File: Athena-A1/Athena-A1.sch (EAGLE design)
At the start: 86 parts, among them J1 MF-CON-MICROUSB-RIGHT, J2 TC2030-IDC-NL, J3 MF-CON-2.54mm-01x08, J4 MF-CON-2.54mm-01x08, J5 MF-CON-2.54mm-01x07, SW1 MF-SW-TACT-6MM, SW2 MF-SW-TACT-6MM, U1 PRTR5V0U2X,215, U2 MCP73831T-2ACI/OT, U3 AP2112K-3.3TRG1, U4 RT9080-18GJ5, U5 MK22FN128VLH10, U6 FE310, U7 32MBit, X1 JST 2-Pin, X2 MIKROE_CLICKMINI, Y1 TSX-3225-16.0000MF18X-AC0, Y2 KX3211A0032.768000

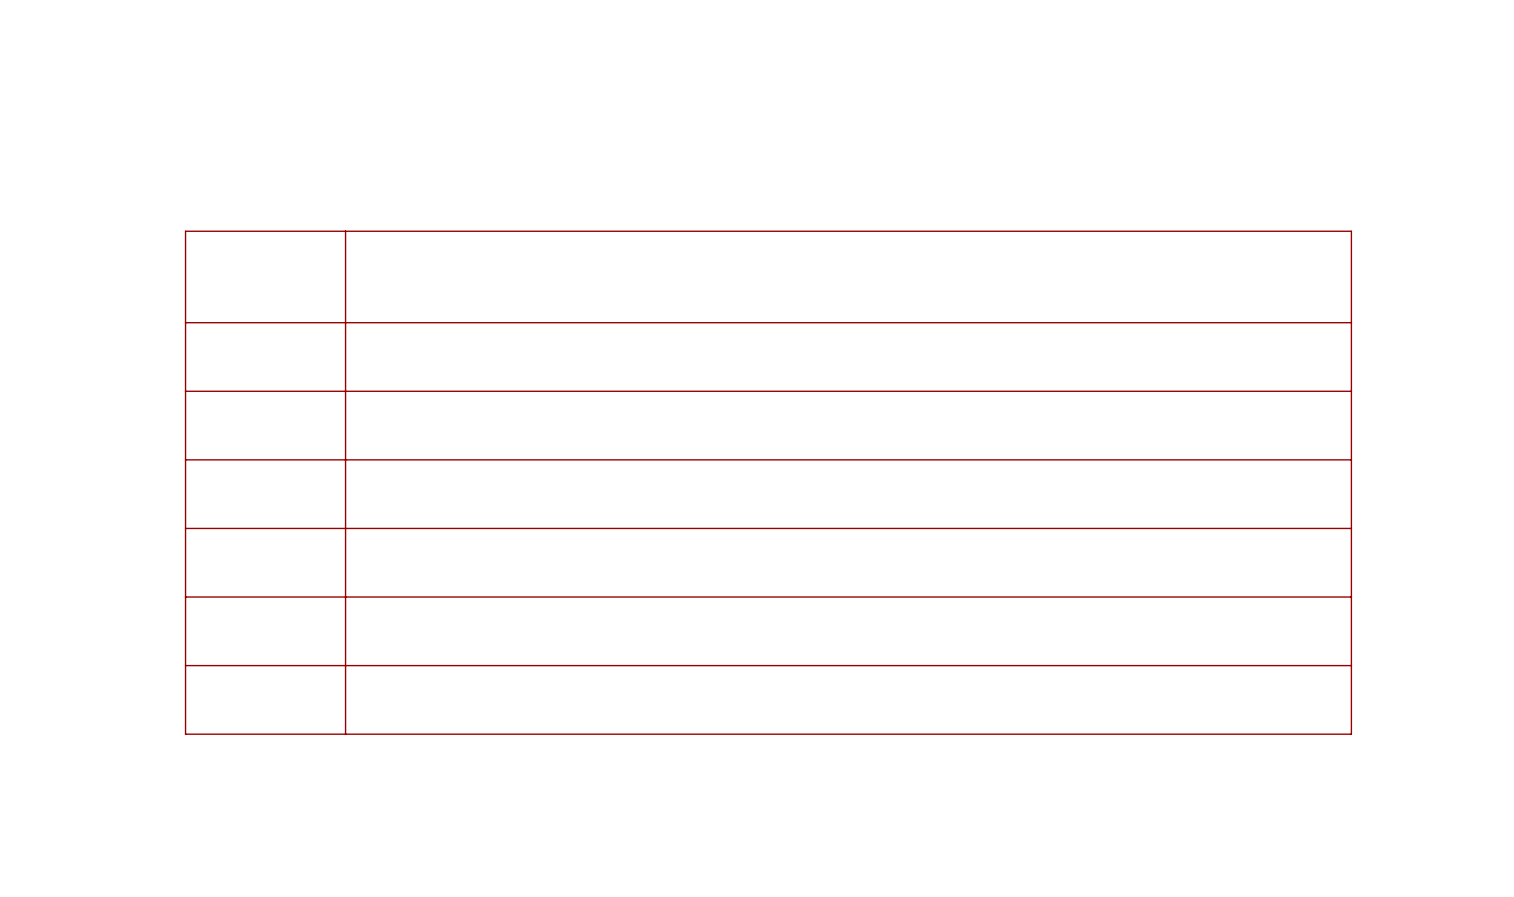
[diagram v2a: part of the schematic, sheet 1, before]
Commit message: Moved pours outside dimension
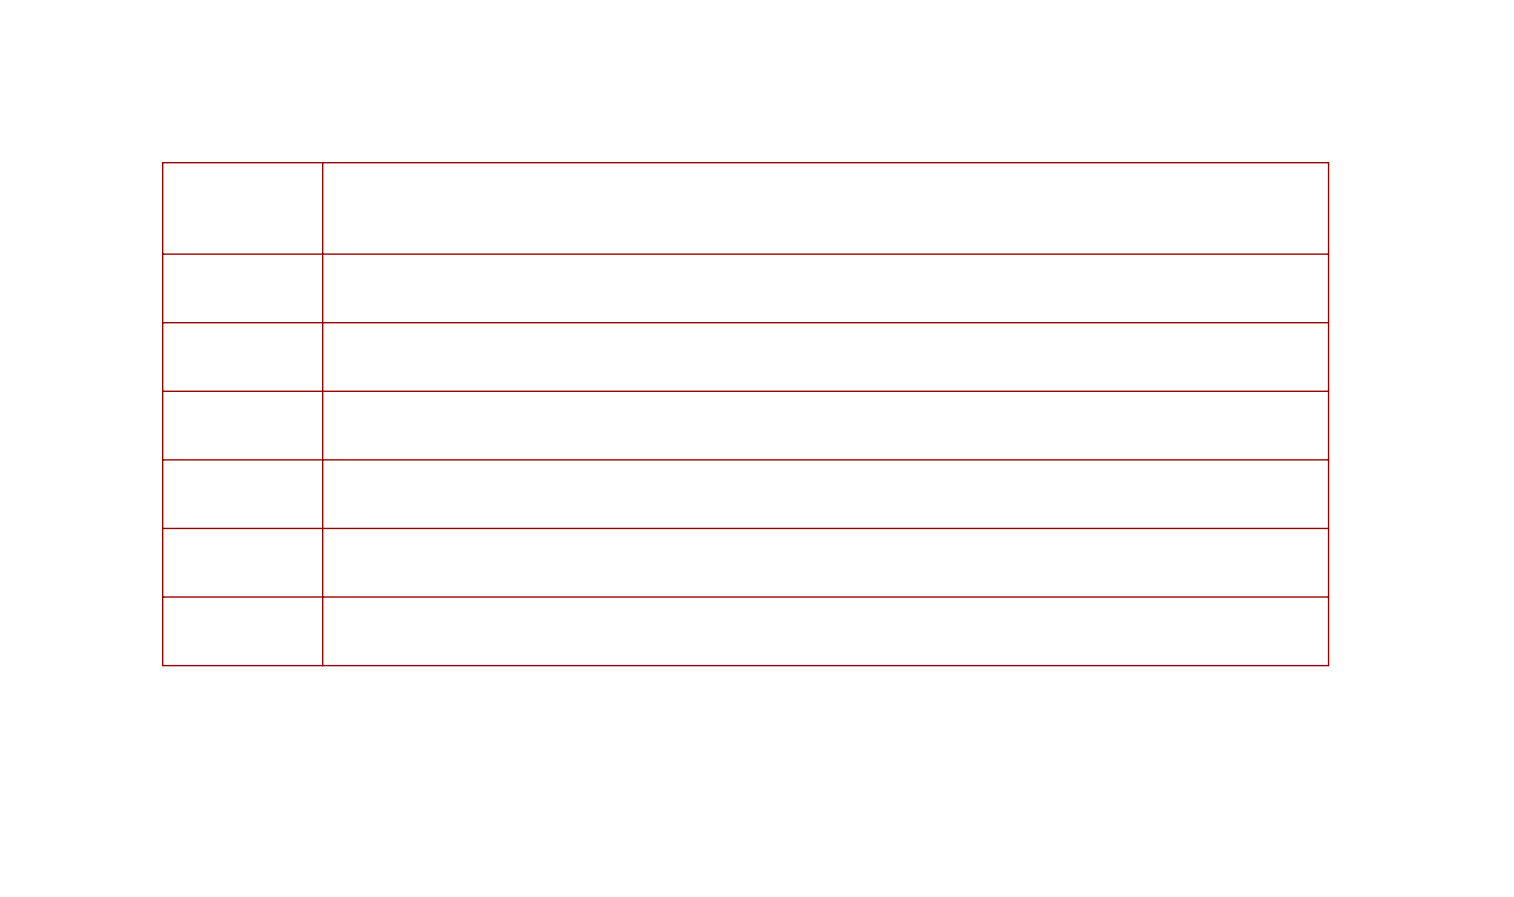
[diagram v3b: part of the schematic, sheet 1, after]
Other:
- note added: "Copyright © 2022 Rice University Permission is hereby granted, free of charge, to any person obtaining a copy of this design and associated documentation files (the “Design”), to deal in the Design without restriction, including without limitation the rights to use, copy, modify, merge, publish, distribute, sublicense, and/or sell copies of the Design, and to permit persons to whom the Design is 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"
- note removed: "ADD A COPYRIGHT AND LICENSE STATEMENT HERE"
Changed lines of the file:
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@@
 <text x="71.12" y="154.94" size="5.08" layer="150">Athena Design Rev. A1 Schematic</text>
 <text x="210.82" y="2.54" size="2.1844" layer="150">Designed in EAGLE 9.6.2.</text>
-<text x="63.5" y="109.22" size="2.54" layer="150" font="vector">The first RISC-V development board at Rice University, featuring the SiFive FE310
+<text x="60.96" y="114.3" size="2.54" layer="150" font="vector">The first RISC-V development board at Rice University, featuring the SiFive FE310
 microprocessor, Athena is a prototyping and experimental platform for education
 and research at Rice.  It is intended to be used in undergraduate lab courses and
 in VIP projects, therefore the design focus is on debug capability and I/O access.</text>
-<text x="114.3" y="91.44" size="2.54" layer="150" ratio="12">July 25, 2022</text>
+<text x="111.76" y="99.06" size="2.54" layer="150" ratio="12">July 25, 2022</text>
 <wire x1="0" y1="0" x2="0" y2="185.42" width="0.508" layer="94"/>
 <wire x1="248.92" y1="185.42" x2="248.92" y2="0" width="0.508" layer="94"/>
 <wire x1="0" y1="185.42" x2="248.92" y2="185.42" width="0.508" layer="94"/>
 <wire x1="0" y1="0" x2="248.92" y2="0" width="0.508" layer="94"/>
-<wire x1="63.5" y1="81.28" x2="81.28" y2="81.28" width="0.1524" layer="94"/>
-<wire x1="81.28" y1="81.28" x2="193.04" y2="81.28" width="0.1524" layer="94"/>
-<wire x1="193.04" y1="81.28" x2="193.04" y2="71.12" width="0.1524" layer="94"/>
-<wire x1="193.04" y1="71.12" x2="193.04" y2="63.5" width="0.1524" layer="94"/>
-<wire x1="193.04" y1="63.5" x2="193.04" y2="55.88" width="0.1524" layer="94"/>
-<wire x1="193.04" y1="55.88" x2="193.04" y2="48.26" width="0.1524" layer="94"/>
-<wire x1="193.04" y1="48.26" x2="193.04" y2="40.64" width="0.1524" layer="94"/>
-<wire x1="193.04" y1="40.64" x2="193.04" y2="33.02" width="0.1524" layer="94"/>
-<wire x1="193.04" y1="33.02" x2="193.04" y2="25.4" width="0.1524" layer="94"/>
-<wire x1="193.04" y1="25.4" x2="81.28" y2="25.4" width="0.1524" layer="94"/>
-<wire x1="81.28" y1="25.4" x2="63.5" y2="25.4" width="0.1524" layer="94"/>
-<wire x1="63.5" y1="25.4" x2="63.5" y2="33.02" width="0.1524" layer="94"/>
-<wire x1="63.5" y1="33.02" x2="63.5" y2="40.64" width="0.1524" layer="94"/>
-<wire x1="63.5" y1="40.64" x2="63.5" y2="48.26" width="0.1524" layer="94"/>
-<wire x1="63.5" y1="48.26" x2="63.5" y2="55.88" width="0.1524" layer="94"/>
-<wire x1="63.5" y1="55.88" x2="63.5" y2="63.5" width="0.1524" layer="94"/>
-<wire x1="63.5" y1="63.5" x2="63.5" y2="71.12" width="0.1524" layer="94"/>
-<wire x1="63.5" y1="71.12" x2="63.5" y2="81.28" width="0.1524" layer="94"/>
-<wire x1="63.5" y1="71.12" x2="193.04" y2="71.12" width="0.1524" layer="94"/>
-<wire x1="81.28" y1="81.28" x2="81.28" y2="25.4" width="0.1524" layer="94"/>
-<wire x1="63.5" y1="63.5" x2="193.04" y2="63.5" width="0.1524" layer="94"/>
-<wire x1="63.5" y1="55.88" x2="193.04" y2="55.88" width="0.1524" layer="94"/>
-<wire x1="63.5" y1="48.26" x2="193.04" y2="48.26" width="0.1524" layer="94"/>
-<wire x1="63.5" y1="40.64" x2="193.04" y2="40.64" width="0.1524" layer="94"/>
-<wire x1="63.5" y1="33.02" x2="193.04" y2="33.02" width="0.1524" layer="94"/>
-<text x="66.04" y="73.66" size="2.54" layer="150" font="vector" ratio="12">Sheet</text>
-<text x="66.04" y="66.04" size="2.54" layer="150" ratio="12">1</text>
-<text x="86.36" y="58.42" size="2.54" layer="150" ratio="12">Power: USB, Charging, Voltage Regulators</text>
-<text x="86.36" y="50.8" size="2.54" layer="150" ratio="12">Debug Control: MK22 Processor</text>
-<text x="86.36" y="66.04" size="2.54" layer="150" ratio="12">Cover Page</text>
-<text x="86.36" y="43.18" size="2.54" layer="150" ratio="12">Main Processor: SiFive FE310, the RISC-V MCU</text>
-<text x="86.36" y="35.56" size="2.54" layer="150" ratio="12">Peripherals: Oscillators, Flash Memory</text>
-<text x="86.36" y="27.94" size="2.54" layer="150" ratio="12">I/O Headers: mikroBus-Compatible, GPIO, and Power; Mechanical</text>
-<text x="66.04" y="58.42" size="2.54" layer="150" ratio="12">2</text>
-<text x="66.04" y="50.8" size="2.54" layer="150" ratio="12">3</text>
-<text x="66.04" y="43.18" size="2.54" layer="150" ratio="12">4</text>
-<text x="66.04" y="35.56" size="2.54" layer="150" ratio="12">5</text>
-<text x="66.04" y="27.94" size="2.54" layer="150" ratio="12">6</text>
-<text x="86.36" y="73.66" size="2.54" layer="150" font="vector" ratio="12">Description</text>
-<text x="7.62" y="2.54" size="5.08" layer="150" font="vector">ADD A COPYRIGHT AND LICENSE STATEMENT HERE</text>
+<wire x1="60.96" y1="88.9" x2="78.74" y2="88.9" width="0.1524" layer="94"/>
+<wire x1="78.74" y1="88.9" x2="190.5" y2="88.9" width="0.1524" layer="94"/>
+<wire x1="190.5" y1="88.9" x2="190.5" y2="78.74" width="0.1524" layer="94"/>
+<wire x1="190.5" y1="78.74" x2="190.5" y2="71.12" width="0.1524" layer="94"/>
+<wire x1="190.5" y1="71.12" x2="190.5" y2="63.5" width="0.1524" layer="94"/>
+<wire x1="190.5" y1="63.5" x2="190.5" y2="55.88" width="0.1524" layer="94"/>
+<wire x1="190.5" y1="55.88" x2="190.5" y2="48.26" width="0.1524" layer="94"/>
+<wire x1="190.5" y1="48.26" x2="190.5" y2="40.64" width="0.1524" layer="94"/>
+<wire x1="190.5" y1="40.64" x2="190.5" y2="33.02" width="0.1524" layer="94"/>
+<wire x1="190.5" y1="33.02" x2="78.74" y2="33.02" width="0.1524" layer="94"/>
+<wire x1="78.74" y1="33.02" x2="60.96" y2="33.02" width="0.1524" layer="94"/>
+<wire x1="60.96" y1="33.02" x2="60.96" y2="40.64" width="0.1524" layer="94"/>
+<wire x1="60.96" y1="40.64" x2="60.96" y2="48.26" width="0.1524" layer="94"/>
+<wire x1="60.96" y1="48.26" x2="60.96" y2="55.88" width="0.1524" layer="94"/>
+<wire x1="60.96" y1="55.88" x2="60.96" y2="63.5" width="0.1524" layer="94"/>
+<wire x1="60.96" y1="63.5" x2="60.96" y2="71.12" width="0.1524" layer="94"/>
+<wire x1="60.96" y1="71.12" x2="60.96" y2="78.74" width="0.1524" layer="94"/>
+<wire x1="60.96" y1="78.74" x2="60.96" y2="88.9" width="0.1524" layer="94"/>
+<wire x1="60.96" y1="78.74" x2="190.5" y2="78.74" width="0.1524" layer="94"/>
+<wire x1="78.74" y1="88.9" x2="78.74" y2="33.02" width="0.1524" layer="94"/>
+<wire x1="60.96" y1="71.12" x2="190.5" y2="71.12" width="0.1524" layer="94"/>
+<wire x1="60.96" y1="63.5" x2="190.5" y2="63.5" width="0.1524" layer="94"/>
+<wire x1="60.96" y1="55.88" x2="190.5" y2="55.88" width="0.1524" layer="94"/>
+<wire x1="60.96" y1="48.26" x2="190.5" y2="48.26" width="0.1524" layer="94"/>
+<wire x1="60.96" y1="40.64" x2="190.5" y2="40.64" width="0.1524" layer="94"/>
+<text x="63.5" y="81.28" size="2.54" layer="150" font="vector" ratio="12">Sheet</text>
+<text x="63.5" y="73.66" size="2.54" layer="150" ratio="12">1</text>
+<text x="83.82" y="66.04" size="2.54" layer="150" ratio="12">Power: USB, Charging, Voltage Regulators</text>
+<text x="83.82" y="58.42" size="2.54" layer="150" ratio="12">Debug Control: MK22 Processor</text>
+<text x="83.82" y="73.66" size="2.54" layer="150" ratio="12">Cover Page</text>
+<text x="83.82" y="50.8" size="2.54" layer="150" ratio="12">Main Processor: SiFive FE310, the RISC-V MCU</text>
+<text x="83.82" y="43.18" size="2.54" layer="150" ratio="12">Peripherals: Oscillators, Flash Memory</text>
+<text x="83.82" y="35.56" size="2.54" layer="150" ratio="12">I/O Headers: mikroBus-Compatible, GPIO, and Power; Mechanical</text>
+<text x="63.5" y="66.04" size="2.54" layer="150" ratio="12">2</text>
+<text x="63.5" y="58.42" size="2.54" layer="150" ratio="12">3</text>
+<text x="63.5" y="50.8" size="2.54" layer="150" ratio="12">4</text>
+<text x="63.5" y="43.18" size="2.54" layer="150" ratio="12">5</text>
+<text x="63.5" y="35.56" size="2.54" layer="150" ratio="12">6</text>
+<text x="83.82" y="81.28" size="2.54" layer="150" font="vector" ratio="12">Description</text>
+<text x="7.62" y="5.08" size="1.778" layer="150" font="vector">Copyright © 2022 Rice University
+Permission is hereby granted, free of charge, to any person obtaining a copy of this design and associated documentation files (the “Design”), to deal in  the Design without restriction, including without
+limitation the rights to use, copy, modify, merge, publish, distribute, sublicense, and/or sell copies of the  Design, and to permit persons to whom the Design is furnished to do so, subject to the following
+conditions: The above copyright notice and this permission notice shall be included in all copies or substantial portions of the Design.
+The Design is provided "as is", without warranty of any kind, express of implied, including but not limited to the warranties of merchantability, fitness for a particular purpose and noninfringement. In no
+event shall the authors or copyright holders be liable for any claim, damages or other liability, whether in an action of contract, tort or otherwise, arising from, out of, or in connection with the Design or
+the use or other dealings in the Design.</text>
 </plain>
 <instances>

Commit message: Athena A1 final
Minor board cleanup
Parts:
- removed X2: MIKROE_CLICKMINI, OSDZU3_ref_dsn:MIKROE_CLICKMINI
- renumbered ON/OFF to SW3
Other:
- note added: "October 1, 2022"
- note removed: "July 25, 2022"
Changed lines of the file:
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@@
 <part name="GND29" library="Athena-A1" deviceset="GND" device=""/>
 <part name="GND1" library="Athena-A1" deviceset="GND" device=""/>
-<part name="X2" library="OSDZU3_ref_dsn" deviceset="MIKROE_CLICK" device="MINI"/>
-<part name="ON/OFF" library="Athena-A1" deviceset="PCM12SMTR" device=""/>
+<part name="SW3" library="Athena-A1" deviceset="PCM12SMTR" device=""/>
 <part name="R4" library="Athena-A1" deviceset="RESISTOR" device="_0402" value="100k"/>
 <part name="GND2" library="Athena-A1" deviceset="GND" device=""/>
@@
 and research at Rice.  It is intended to be used in undergraduate lab courses and
 in VIP projects, therefore the design focus is on debug capability and I/O access.</text>
-<text x="111.76" y="99.06" size="2.54" layer="150" ratio="12">July 25, 2022</text>
+<text x="111.76" y="99.06" size="2.54" layer="150" ratio="12">October 1, 2022</text>
 <wire x1="0" y1="0" x2="0" y2="185.42" width="0.508" layer="94"/>
 <wire x1="248.92" y1="185.42" x2="248.92" y2="0" width="0.508" layer="94"/>
@@
 <attribute name="REV" x="236.22" y="6.604" size="2.7432" layer="94" font="vector"/>
 </instance>
-<instance part="ON/OFF" gate="G$1" x="73.66" y="71.12" smashed="yes">
+<instance part="SW3" gate="G$1" x="73.66" y="71.12" smashed="yes">
 <attribute name="NAME" x="71.115609375" y="61.218609375" size="2.54" layer="95"/>
 <attribute name="VALUE" x="71.01865" y="56.378140625" size="2.54" layer="96"/>
@@
 <segment>
 <pinref part="R3" gate="G$1" pin="P$1"/>
-<pinref part="ON/OFF" gate="G$1" pin="1"/>
+<pinref part="SW3" gate="G$1" pin="1"/>
 <wire x1="63.5" y1="73.66" x2="66.04" y2="73.66" width="0.1524" layer="91"/>
 </segment>
@@
 <net name="N$16" class="0">
 <segment>
-<pinref part="ON/OFF" gate="G$1" pin="2"/>
+<pinref part="SW3" gate="G$1" pin="2"/>
 <pinref part="U3" gate="G$1" pin="EN"/>
 <wire x1="81.28" y1="71.12" x2="81.28" y2="73.66" width="0.1524" layer="91"/>
@@
 <net name="N$17" class="0">
 <segment>
-<pinref part="ON/OFF" gate="G$1" pin="3"/>
+<pinref part="SW3" gate="G$1" pin="3"/>
 <pinref part="R4" gate="G$1" pin="P$1"/>
 <wire x1="66.04" y1="68.58" x2="63.5" y2="68.58" width="0.1524" layer="91"/>
@@
 <attribute name="VALUE" x="81.28" y="37.846" size="2.54" layer="96" align="top-center"/>
 </instance>
-<instance part="X2" gate="G$1" x="152.4" y="99.06" smashed="yes">
-<attribute name="NAME" x="152.4" y="99.06" size="1.778" layer="95"/>
-<attribute name="VALUE" x="152.4" y="71.12" size="1.778" layer="96"/>
-</instance>
 </instances>
